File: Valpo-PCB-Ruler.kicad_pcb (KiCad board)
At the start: 2 copper layers, 203.2 x 38.1 mm, 52 parts

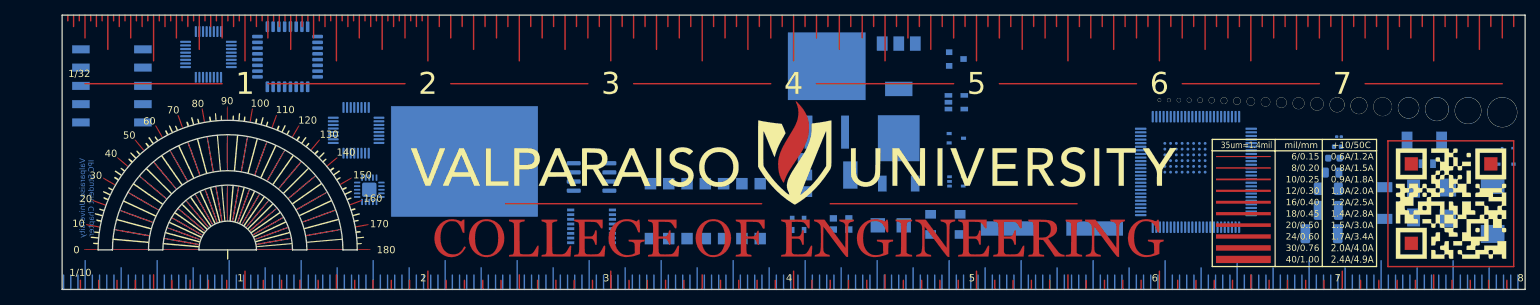
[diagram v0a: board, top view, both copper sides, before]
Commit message: Update basic design
Reduced size of ruler from 8in to 6in. Adjusted positioning of front masks and screens to match new size. Removed most of the references on the back to make room for the new circuitry to be included. Found initial components for USB circuitry (using ATtiny85).
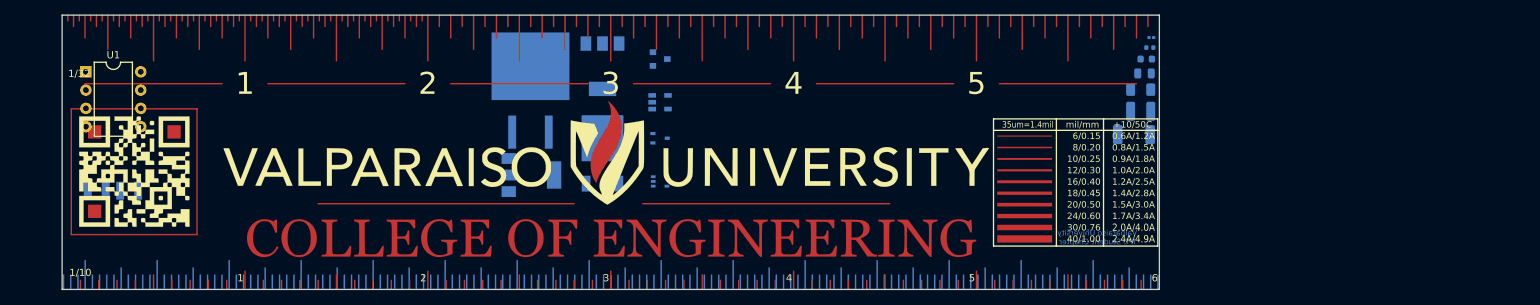
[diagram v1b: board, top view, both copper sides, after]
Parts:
- removed 2.5x2: Oscillator_SMD_Abracon_ASDMB-4Pin_2.5x2.0mm, Oscillator:Oscillator_SMD_Abracon_ASDMB-4Pin_2.5x2.0mm
- removed 3.2x2.4: Oscillator_SMD_EuroQuartz_XO32-4Pin_3.2x2.5mm, Oscillator:Oscillator_SMD_EuroQuartz_XO32-4Pin_3.2x2.5mm
- removed 5x3.2: Oscillator_SMD_Fordahl_DFAS15-4Pin_5.0x3.2mm, Oscillator:Oscillator_SMD_Fordahl_DFAS15-4Pin_5.0x3.2mm
- removed 5x3.2: Crystal_SMD_Qantek_QC5CB-2Pin_5x3.2mm, Crystal:Crystal_SMD_Qantek_QC5CB-2Pin_5x3.2mm
- removed BGA 0.8mm: BGA-48_8.0x9.0mm_Layout6x8_P0.8mm, Package_BGA:BGA-48_8.0x9.0mm_Layout6x8_P0.8mm
- removed DIP 14 Pin: DIP-14_W7.62mm_SMDSocket_SmallPads, Package_DIP:DIP-14_W7.62mm_SMDSocket_SmallPads
- removed Dip Switch 5: SW_DIP_SPSTx05_Slide_9.78x14.88mm_W8.61mm_P2.54mm, Button_Switch_SMD:SW_DIP_SPSTx05_Slide_9.78x14.88mm_W8.61mm_P2.54mm
- removed the G*** at (73.7, 96.1) (x2)
- removed the G*** at (73.8, 96.1) (x4)
- removed HC49: Crystal_SMD_HC49-SD_HandSoldering, Crystal:Crystal_SMD_HC49-SD_HandSoldering
- removed MELF: D_MELF, Diode_SMD:D_MELF
- removed MicroMELF: D_MicroMELF, Diode_SMD:D_MicroMELF
- removed QFN: QFN-20-1EP_3.5x3.5mm_P0.5mm_EP2x2mm, Package_DFN_QFN:QFN-20-1EP_3.5x3.5mm_P0.5mm_EP2x2mm
- removed QFP, QFP32: LQFP-32_5x5mm_P0.5mm, Package_QFP:LQFP-32_5x5mm_P0.5mm
- removed QFP32: LQFP-32_7x7mm_P0.8mm, Package_QFP:LQFP-32_7x7mm_P0.8mm
- removed QPF100: LQFP-100_14x14mm_P0.5mm, Package_QFP:LQFP-100_14x14mm_P0.5mm
- removed SC80: D_SC-80, Diode_SMD:D_SC-80
- removed SMA: D_SMA, Diode_SMD:D_SMA
- removed SMB: D_SMB, Diode_SMD:D_SMB
- removed SMC: D_SMC, Diode_SMD:D_SMC
- removed SOD 128: D_SOD-128, Diode_SMD:D_SOD-128
- removed SOD 323: D_SOD-323, Diode_SMD:D_SOD-323
- removed SOIC: SOIC-8_3.9x4.9mm_P1.27mm, Package_SO:SOIC-8_3.9x4.9mm_P1.27mm
- removed SSOP: SSOP-16_4.4x5.2mm_P0.65mm, Package_SO:SSOP-16_4.4x5.2mm_P0.65mm
- added U1: ATtiny85-20PU, Package_DIP:DIP-8_W7.62mm, F.Cu at (54.1, 71.4)
- added U2: USB_Board, Valpo-PCB-Ruler-FP:USB_Board, B.Cu at (58.2, 86.6)
- moved G*** 182.9 mm to (60.7, 85.3) (x3)
- moved SOT223 41.1 mm to (116.0, 85.7)
- moved SOT223 41.1 mm to (125.9, 70.6)
- moved SOT23 41.1 mm to (133.9, 69.6)
- moved SOT23-5 41.1 mm to (133.9, 75.6)
- moved SOT323 41.1 mm to (133.9, 80.6)
- moved SOT353 41.1 mm to (133.9, 86.6)
- moved TO252 41.1 mm to (125.9, 82.7)
- moved TO263 41.1 mm to (115.9, 74.0)
- moved 0201 29.5 mm to (202.1, 66.6)
- moved 0402 29.5 mm to (201.9, 68.0)
- moved 0805 29.5 mm to (201.1, 71.6)
- moved 2010 29.5 mm to (199.7, 80.1)
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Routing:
- net (no net): vias 20 -> 0
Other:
- board size 203.2 x 38.1 mm -> 152.4 x 38.1 mm
- board text removed: ".45"
- board text removed: ".51"
- board text removed: ".57"
- board text removed: "0.5mm Pitch"
- board text removed: "0.6"
- board text removed: "0.7"
- board text removed: "0.8"
- board text removed: "0.8mm Pitch"
- board text removed: "0.9"
- board text removed: "1.0"
- board text removed: "1.2"
- board text removed: "1.3"
- board text removed: "1.5"
- board text removed: "1.6"
- board text removed: "1.8"
- board text removed: "100"
- board text removed: "102"
- board text removed: "110"
- board text removed: "114"
- board text removed: "120"
- board text removed: "128"
- board text removed: "130"
- board text removed: "140"
- board text removed: "144"
- board text removed: "150"
- board text removed: "16"
- board text removed: "160"
- board text removed: "162"
- board text removed: "17"
- board text removed: "170"
- board text removed: "18"
- board text removed: "180"
- board text removed: "19"
- board text removed: "2.0"
- board text removed: "2.3"
- board text removed: "2.6"
- board text removed: "2.9"
- board text removed: "20"
- board text removed: "21"
- board text removed: "22"
- board text removed: "23"
- board text removed: "24"
- board text removed: "25"
- board text removed: "28"
- board text removed: "3.3"
- board text removed: "3.7"
- board text removed: "30"
- board text removed: "32"
- board text removed: "36"
- board text removed: "4.1"
- board text removed: "40"
- board text removed: "45"
- board text removed: "50"
- board text removed: "51"
- board text removed: "57"
- board text removed: "60"
- board text removed: "64"
- board text removed: "70"
- board text removed: "72"
- board text removed: "80"
- board text removed: "90"
- board text removed: "91"
- board text removed: "AWG"
- board text removed: "Diodes"
- board text removed: "fabid: JLCJLCJLCJLC"
- board text removed: "mil"
- board text removed: "mm"

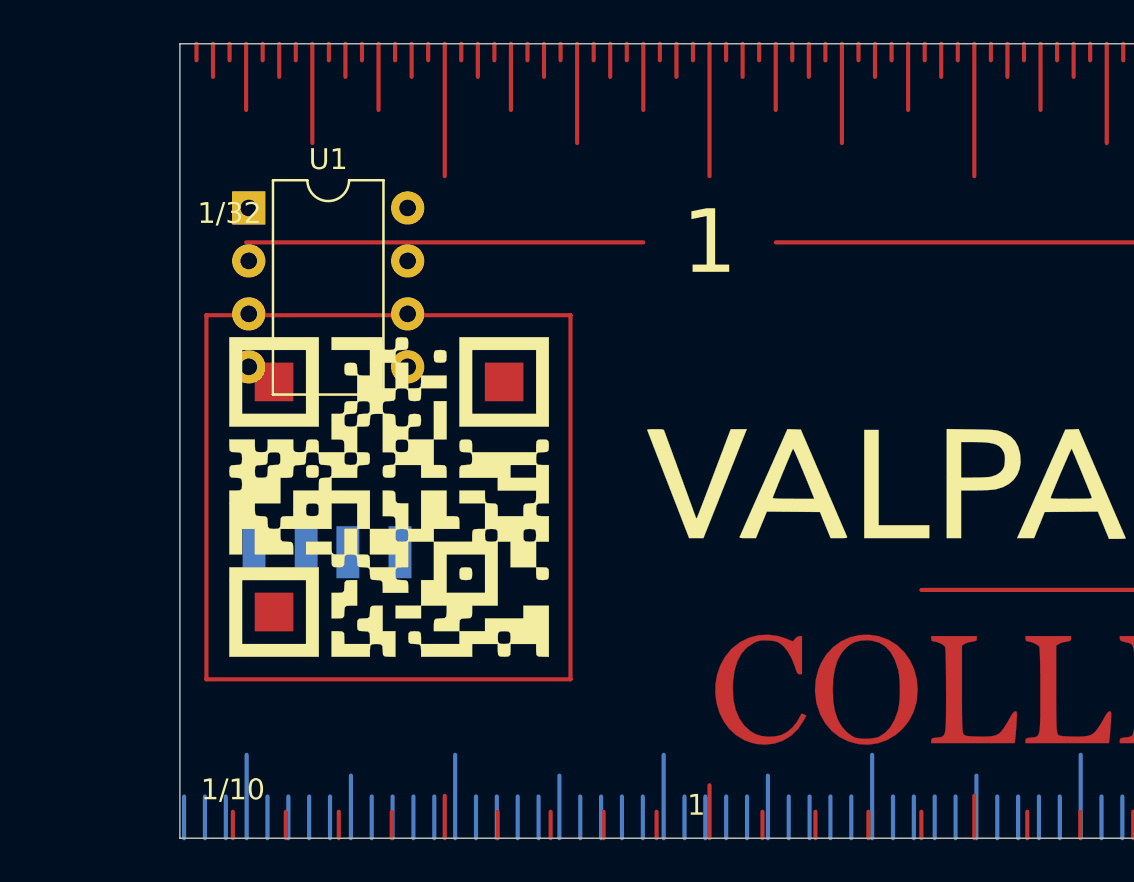
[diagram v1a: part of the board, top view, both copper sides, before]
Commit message: Layout Set
Set out layout and schematics for both LCD and push-buttons. Users will have the option to use either or depending on which solder bridges they connect. Board USB also added to the device, may need to change which side of the board the traces are on if buttons/LCD are not visible.
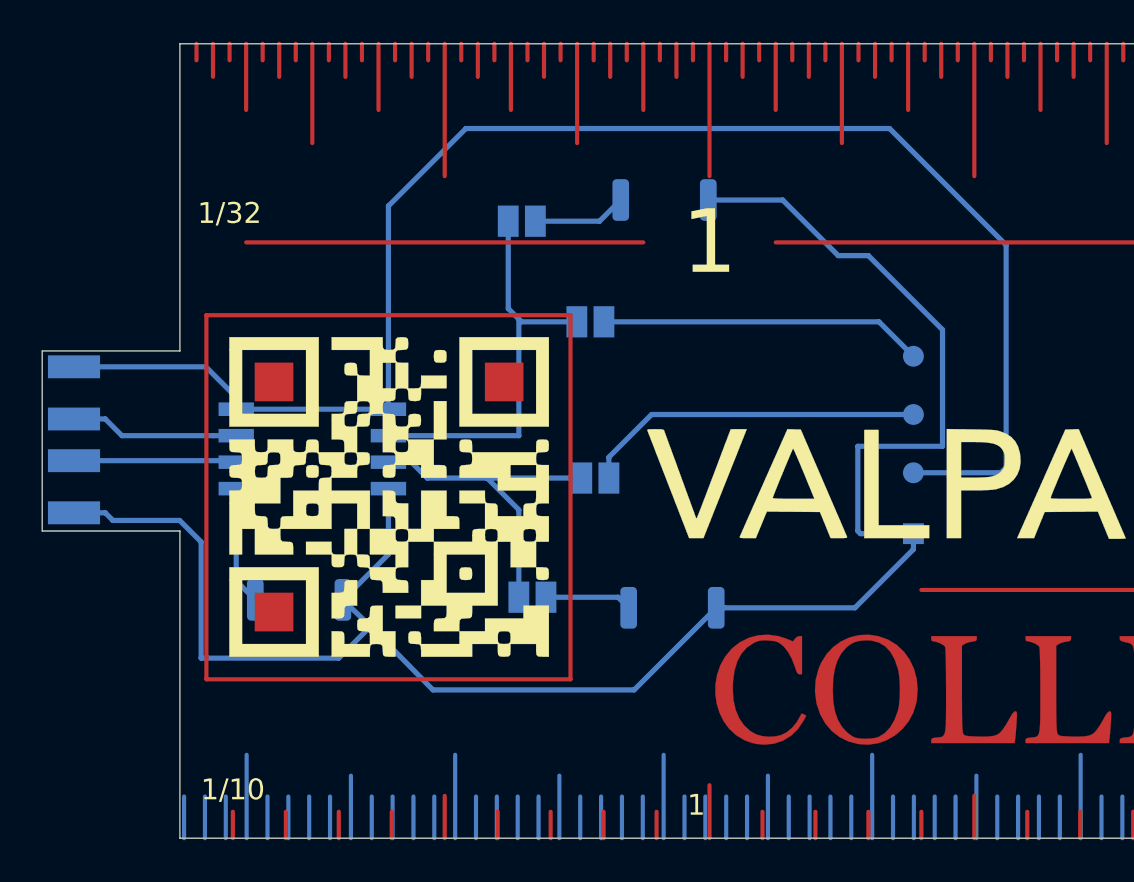
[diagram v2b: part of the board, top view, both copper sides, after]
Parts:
- removed U1: ATtiny85-20PU, Package_DIP:DIP-8_W7.62mm
- added JP1: SolderJumper_2_Open, Jumper:SolderJumper-2_P1.3mm_Open_Pad1.0x1.5mm, B.Cu at (67.2, 72.0)
- added JP2: SolderJumper_2_Open, Jumper:SolderJumper-2_P1.3mm_Open_Pad1.0x1.5mm, B.Cu at (67.7, 90.0)
- added JP3: SolderJumper_2_Open, Jumper:SolderJumper-2_P1.3mm_Open_Pad1.0x1.5mm, B.Cu at (70.5, 76.8)
- added JP4: SolderJumper_2_Open, Jumper:SolderJumper-2_P1.3mm_Open_Pad1.0x1.5mm, B.Cu at (70.7, 84.3)
- added SW1: SW_Push, Button_Switch_SMD:SW_Push_SPST_NO_Alps_SKRK, B.Cu at (56.5, 90.2)
- added SW2: SW_Push, Button_Switch_SMD:SW_Push_SPST_NO_Alps_SKRK, B.Cu at (74.0, 71.0)
- added SW3: SW_Push, Button_Switch_SMD:SW_Push_SPST_NO_Alps_SKRK, B.Cu at (74.4, 90.6)
- added TP1: LCD_DAT, TestPoint:TestPoint_Pad_D1.0mm, B.Cu at (86.0, 78.5)
- added TP2: LCD_CLK, TestPoint:TestPoint_Pad_D1.0mm, B.Cu at (86.0, 81.3)
- added TP3: LCD_VCC, TestPoint:TestPoint_Pad_D1.0mm, B.Cu at (86.0, 84.1)
- added TP4: LCD_GND, TestPoint:TestPoint_Pad_1.0x1.0mm, B.Cu at (86.0, 87.0)
- added U3: ATtiny85-20SU, Package_SO:SOIJ-8_5.3x5.3mm_P1.27mm, B.Cu at (57.1, 82.9)
- moved U2 11.8 mm to (47.0, 82.8), turned to 270 degrees
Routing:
- net GND: track 0.00 -> 90.2 mm
- net +5V: track 0.00 -> 74.7 mm
- net /PB3: track 0.00 -> 19.6 mm
- net Net-(JP4-Pad2): track 0.00 -> 16.5 mm
- net /PB4: track 0.00 -> 15.9 mm
- net Net-(JP3-Pad2): track 0.00 -> 15.5 mm
- net /D+: track 0.00 -> 8.11 mm
- net /D-: track 0.00 -> 7.81 mm
- net Net-(SW1-Pad1): track 0.00 -> 5.71 mm
- net Net-(JP1-Pad2): track 0.00 -> 4.51 mm
- net Net-(JP2-Pad2): track 0.00 -> 4.18 mm
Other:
- board size 152.4 x 38.1 mm -> 159 x 38.1 mm
- board text added: "Designed By Jacob Leazott Updated By Josh Chica"
- board text removed: "Designed By Jacob Leazott"

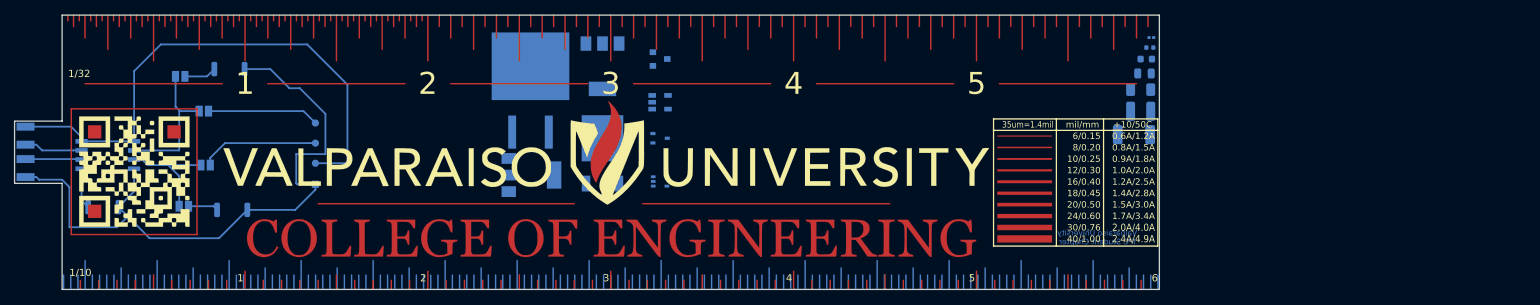
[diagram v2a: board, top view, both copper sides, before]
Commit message: Reverse USB side
Moved the USB to be on the other side of the board to maintain the sanctity of the zero on the left side (for the imperial units).
Reduced transistor diagrams to not some of the smaller diagrams. Added additional hardware to allow the ATtiny to work with USB.
Added some Mechanical engineering focused constants (Avogadro's Number, Gas Constant, Accl due to gravity in metric & imperial)
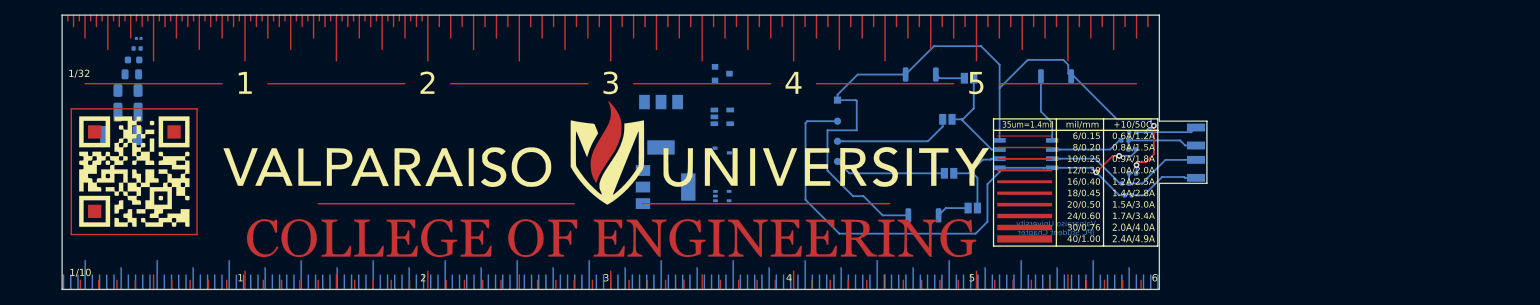
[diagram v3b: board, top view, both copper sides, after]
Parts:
- removed TO252: TO-252-2, Package_TO_SOT_SMD:TO-252-2
- removed TO263: TO-263-2, Package_TO_SOT_SMD:TO-263-2
- added D1: 3.6 Zener, Diode_SMD:D_0402_1005Metric, B.Cu at (199.5, 85.5)
- added D2: D, Diode_SMD:D_0402_1005Metric, B.Cu at (198.9, 88.5)
- added D3: 3.6 Zener, Diode_SMD:D_0402_1005Metric, B.Cu at (199.5, 79.8)
- added R1: 68, Resistor_SMD:R_0402_1005Metric, B.Cu at (198.5, 86.9)
- added R2: 1K5, Resistor_SMD:R_0402_1005Metric, B.Cu at (199.4, 82.2)
- added R3: 68, Resistor_SMD:R_0402_1005Metric, B.Cu at (198.4, 80.9)
- moved U2 160.0 mm to (207.0, 82.3), turned to 90 degrees
- moved 0603 140.7 mm to (60.7, 69.7)
- moved 0805 140.7 mm to (60.5, 71.7)
- moved 1206 140.7 mm to (59.9, 74.0)
- moved 1210 140.7 mm to (59.9, 77.0)
- moved 2010 140.7 mm to (59.0, 80.2)
- moved 0201 140.7 mm to (61.4, 66.7)
- moved 0402 140.7 mm to (61.2, 68.1)
- moved SW1 133.6 mm to (188.8, 72.0)
- moved U3 127.5 mm to (184.7, 82.8), turned to 0 degrees
- moved JP1 111.6 mm to (177.3, 90.3), turned to 180 degrees
- moved JP2 110.5 mm to (176.8, 72.3), turned to 180 degrees
- moved JP3 103.9 mm to (174.0, 85.5), turned to 180 degrees
- moved JP4 103.2 mm to (173.8, 78.0), turned to 180 degrees
- moved SW2 98.5 mm to (170.4, 91.3), turned to 180 degrees
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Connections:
- U2 pad 1: +5V -> Net-(D2-Pad2)
- U2 pad 2: /D+ -> Net-(D1-Pad1)
- U2 pad 3: /D- -> Net-(D3-Pad1)
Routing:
- net GND: track 90.2 -> 114.1 mm, vias 0 -> 2
- net Net-(D1-Pad1): track 0.00 -> 12.4 mm
- net Net-(D3-Pad1): track 0.00 -> 12.3 mm
- net Net-(D2-Pad2): track 0.00 -> 10.0 mm
- net /PB3: track 19.6 -> 12.8 mm
- net Net-(SW1-Pad1): track 5.71 -> 9.54 mm
- net /D+: track 8.11 -> 11.1 mm
- net +5V: track 74.7 -> 77.3 mm, vias 0 -> 2
- net /D-: track 7.81 -> 10.1 mm
- net /PB4: track 15.9 -> 14.9 mm
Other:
- outline, holes or cut-outs redrawn
- board text added: "-1"
- board text added: "-2"
- board text added: "23"
- board text added: "Accelration due to gravity=32.17 ft*s"
- board text added: "Accelration due to gravity=9.8 m*s"
- board text added: "Avogadro's Number=6.022×10 mol"
- board text added: "Gas Constat=8.314 J*K *mol"
- board text removed: "D2PAK"
- board text removed: "DPAK"
